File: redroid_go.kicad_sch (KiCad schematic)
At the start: 97 parts, among them J1 USB4105-GF-A, J2 5051101892, J3 Conn_01x02_Pin, J4 Conn_01x10_Pin, Q1 UMH3N, Q2 PMOS, Q3 UMH3N, SW1 UP, SW10 A, SW11 SW_SPDT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

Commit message: Advances
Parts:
- removed JP1: SolderJumper_3_Bridged12, Jumper:SolderJumper-3_P1.3mm_Bridged12_Pad1.0x1.5mm_NumberLabels, symbol Jumper:SolderJumper_3_Bridged12
- removed unit 2 of Q3
- removed R21: 10k, Resistor_SMD:R_0603_1608Metric_Pad0.98x0.95mm_HandSolder, symbol Device:R_US
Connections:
- net RESET: now also J2.17 (RST)

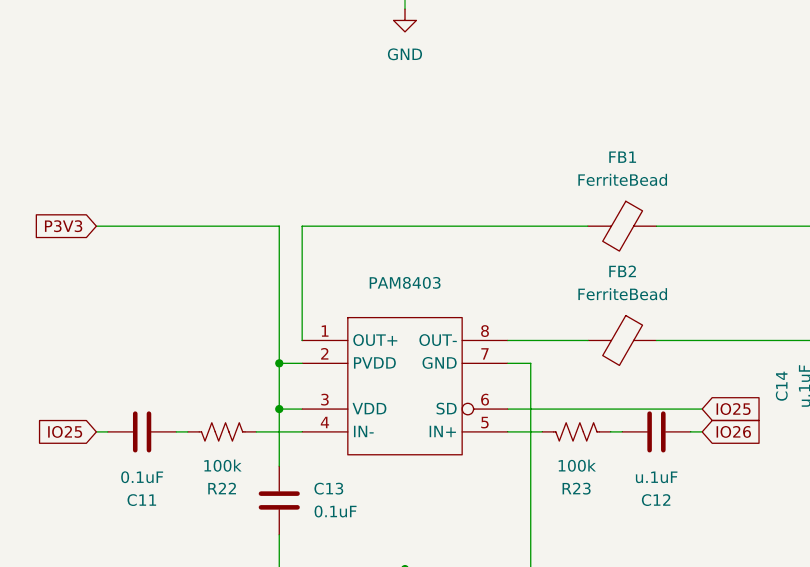
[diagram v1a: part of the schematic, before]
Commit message: Fix audo amplifier IC name
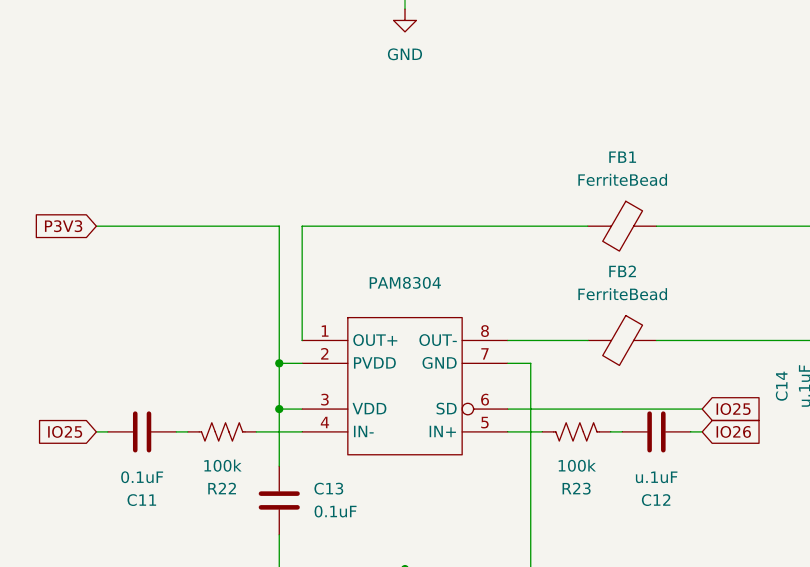
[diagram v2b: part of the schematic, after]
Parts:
- renumbered PAM8403 to PAM8304
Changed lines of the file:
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@@
 		(dnp no)
 		(fields_autoplaced yes)
-		(property "Reference" "PAM8403"
+		(property "Reference" "PAM8304"
 			(at 69.85 209.55 0)
 			(effects
@@
 			(project ""
 				(path "/54323edd-924e-4c99-bcbf-5375689f8e73"
-					(reference "PAM8403")
+					(reference "PAM8304")
 					(unit 1)
 				)

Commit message: Update diode footprint
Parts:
- D1: footprint Diode_SMD:D_SOD-323 -> Diode_SMD:Nexperia_CFP3_SOD-123W
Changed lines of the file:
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@@
 			)
 		)
-		(property "Footprint" "Diode_SMD:D_SOD-323"
+		(property "Footprint" "Diode_SMD:Nexperia_CFP3_SOD-123W"
 			(at 273.05 45.72 0)
 			(effects

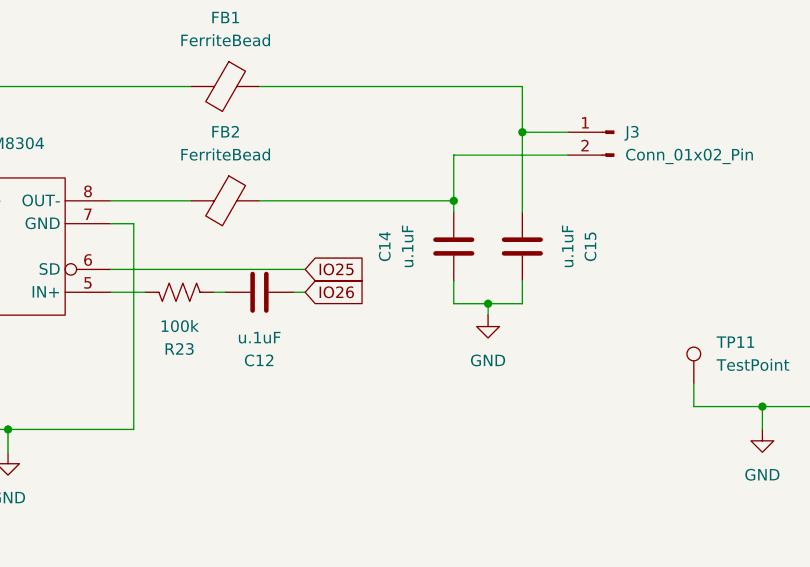
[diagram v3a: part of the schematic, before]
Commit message: Fix values of some capacitors
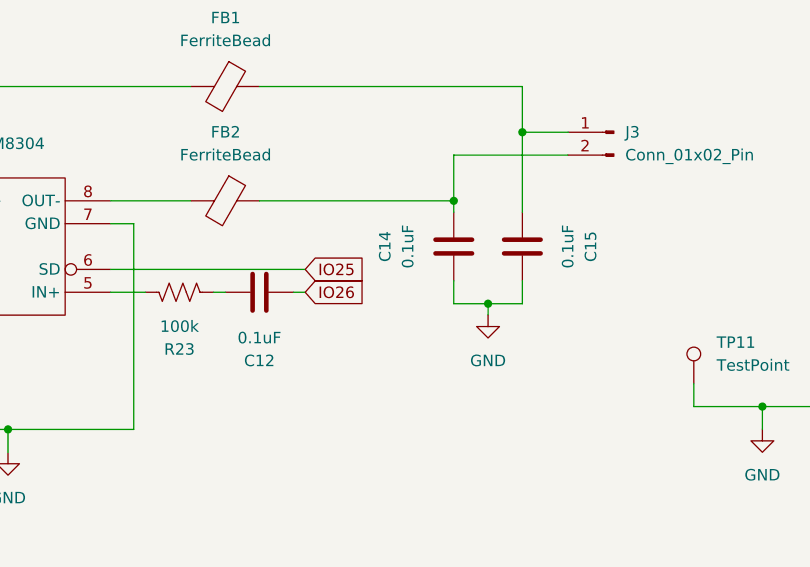
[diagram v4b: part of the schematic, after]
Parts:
- C12, C14, C15: value u.1uF -> 0.1uF
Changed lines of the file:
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@@
 			)
 		)
-		(property "Value" "u.1uF"
+		(property "Value" "0.1uF"
 			(at 132.08 220.98 90)
 			(effects
@@
 			)
 		)
-		(property "Value" "u.1uF"
+		(property "Value" "0.1uF"
 			(at 97.79 231.14 90)
 			(effects
@@
 			)
 		)
-		(property "Value" "u.1uF"
+		(property "Value" "0.1uF"
 			(at 114.3 220.98 90)
 			(effects

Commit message: Change L1 PCB footprint
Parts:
- L1: footprint Inductor_SMD:L_Coilcraft_LPS3010 -> Inductor_SMD:L_Murata_LQH2MCNxxxx02_2.0x1.6mm
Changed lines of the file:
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@@
 			)
 		)
-		(property "Footprint" "Inductor_SMD:L_Coilcraft_LPS3010"
+		(property "Footprint" "Inductor_SMD:L_Murata_LQH2MCNxxxx02_2.0x1.6mm"
 			(at 302.26 52.07 0)
 			(effects
